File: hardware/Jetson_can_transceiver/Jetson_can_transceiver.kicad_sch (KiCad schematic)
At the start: 5 parts, among them U1 MCP2551-I-P, U2 MCP2551-I-P

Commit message: Added realistic footprints to electronic components
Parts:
- C2: footprint (none) -> Capacitor_SMD:C_0805_2012Metric
- R1, R2: footprint (none) -> Resistor_SMD:R_0805_2012Metric
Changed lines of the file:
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@@
 			)
 		)
-		(property "Footprint" ""
+		(property "Footprint" "Capacitor_SMD:C_0805_2012Metric"
 			(at 83.5152 29.21 0)
 			(effects
@@
 			)
 		)
-		(property "Footprint" ""
+		(property "Footprint" "Resistor_SMD:R_0805_2012Metric"
 			(at 107.188 64.77 90)
 			(effects
@@
 			)
 		)
-		(property "Footprint" ""
+		(property "Footprint" "Resistor_SMD:R_0805_2012Metric"
 			(at 60.198 63.5 90)
 			(effects

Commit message: Completed blueprint for 2 transceivers
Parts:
- added J1: Conn_02x20_Odd_Even, symbol Connector_Generic:Conn_02x20_Odd_Even
- added R3, R4: 120R, Resistor_SMD:R_0805_2012Metric, symbol Device:R
- C2: value 100pF -> 100nF
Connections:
- net GND: now also J1.6 (Pin_6)
- net CANL1: now reaches U2.6 (CANL)
- net CANL1: now also R4.2
- net CANH1: now reaches U2.7 (CANH)
- net CANH1: now also R4.1
- net CANL0: now reaches U1.6 (CANL)
- net CANL0: now also R3.2
- net CANH0: now reaches U1.7 (CANH)
- net CANH0: now also R3.1
- net +5V renamed 5V
- net 5V: now also J1.2 (Pin_2)
- net RXD_1 renamed RX0
- net RX0: now also J1.29 (Pin_29)
- net RXD_2 renamed RX1
- net RX1: now also J1.37 (Pin_37)
- net TXD_1 renamed TX0
- net TX0: now also J1.31 (Pin_31)
- net TXD_2 renamed TX1
- net TX1: now also J1.33 (Pin_33)
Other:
- moved on the sheet: R1, R2, U1, U2

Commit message: added footprints
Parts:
- J1: footprint (none) -> Connector_Harwin:Harwin_M20-7812045_2x20_P2.54mm_Vertical
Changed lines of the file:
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@@
 			)
 		)
-		(property "Footprint" ""
+		(property "Footprint" "Connector_Harwin:Harwin_M20-7812045_2x20_P2.54mm_Vertical"
 			(at 83.82 99.06 0)
 			(effects

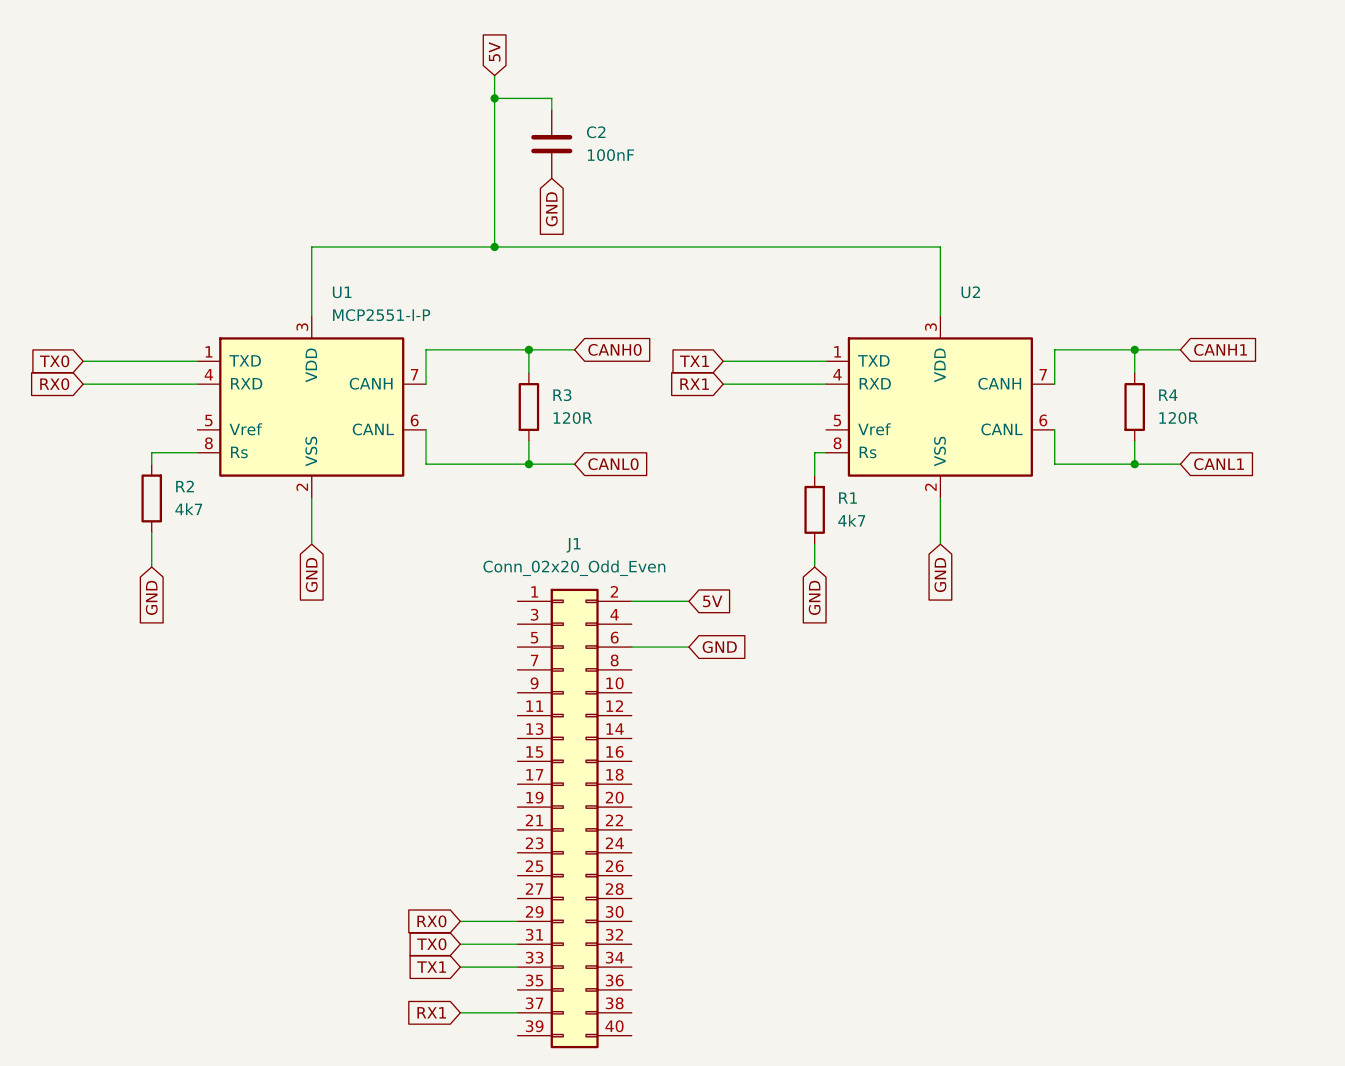
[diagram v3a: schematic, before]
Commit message: Changed from mcp2551 to mcp2542fd, added test points, changed footprint to 0603
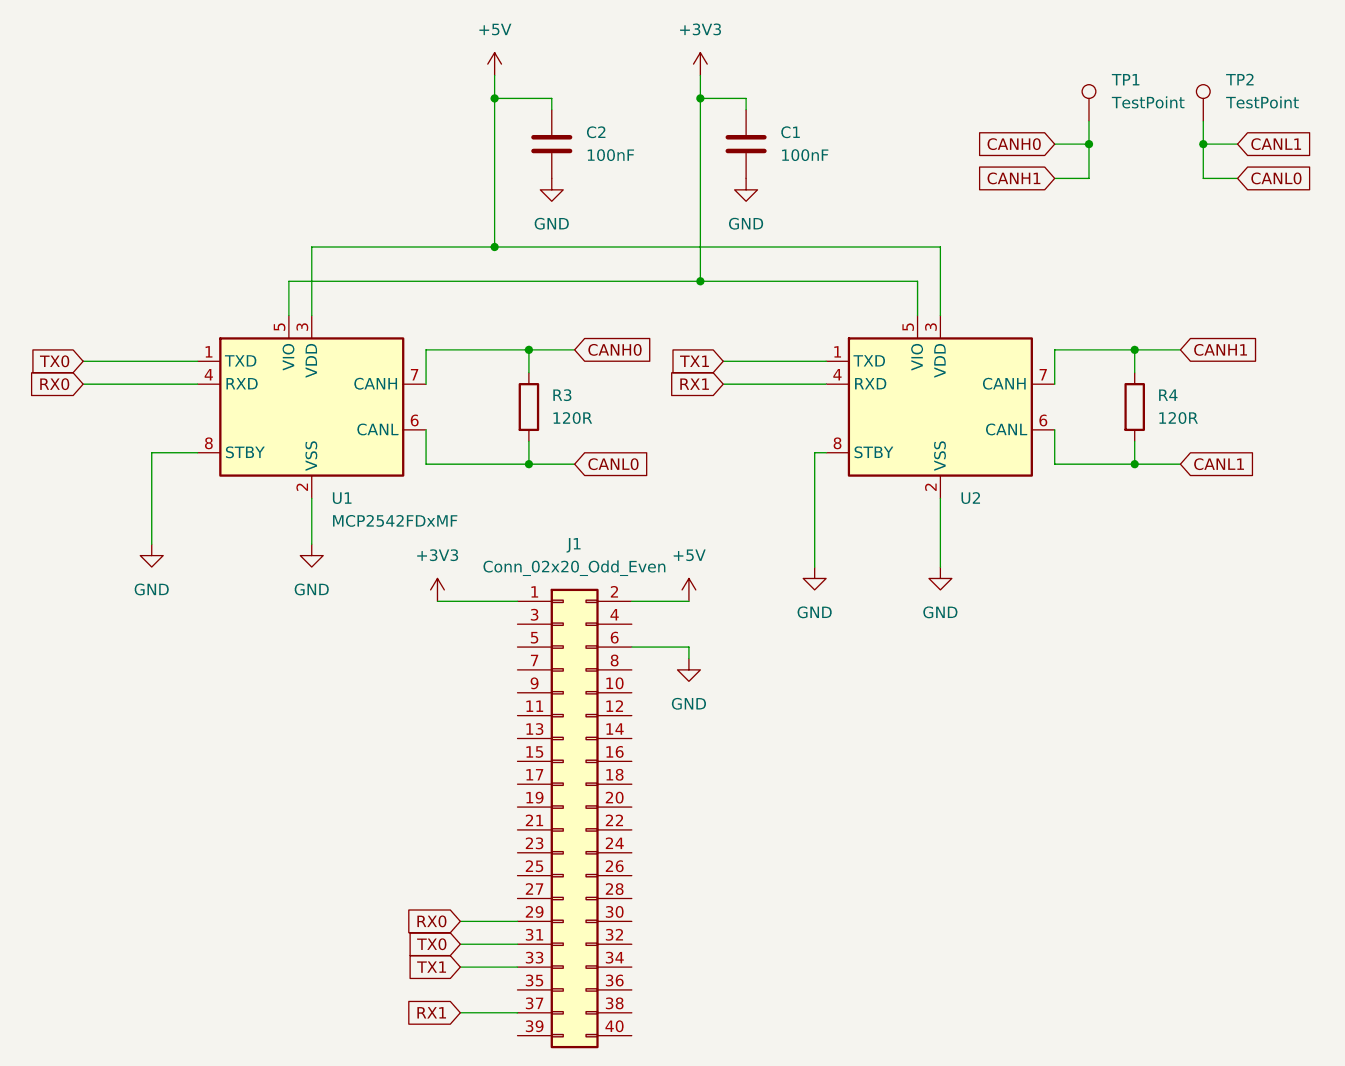
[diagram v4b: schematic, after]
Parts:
- removed R1, R2: 4k7, Resistor_SMD:R_0805_2012Metric, symbol Device:R
- removed U1, U2: MCP2551-I-P, Package_DIP:DIP-8_W7.62mm, symbol Interface_CAN_LIN:MCP2551-I-P
- added C1: 100nF, Capacitor_SMD:C_0603_1608Metric, symbol Device:C
- added TP1, TP2: TestPoint, S1751-46R:HARWIN_S1751-46R, symbol Connector:TestPoint
- added U1, U2: MCP2542FDxMF, Package_DFN_QFN:DFN-8-1EP_3x3mm_P0.65mm_EP1.55x2.4mm, symbol Interface_CAN_LIN:MCP2542FDxMF
- C2: footprint Capacitor_SMD:C_0805_2012Metric -> Capacitor_SMD:C_0603_1608Metric
- R3, R4: footprint Resistor_SMD:R_0805_2012Metric -> Resistor_SMD:R_0603_1608Metric
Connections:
- net CANH1 is gone; now on net CANH0: R4.1
- net CANL1 is gone; now on net CANL0: R4.2
- net CANH0: now also TP1.1, U1.7 (CANH), U2.7 (CANH)
- net CANL0: now also TP2.1, U1.6 (CANL), U2.6 (CANL)
- net GND: now also C1.2, U1.2 (VSS), U1.8 (STBY), U1.9 (VSS), U2.2 (VSS), U2.8 (STBY), U2.9 (VSS)
- net RX0: now also U1.4 (RXD)
- net RX1: now also U2.4 (RXD)
- net TX0: now also U1.1 (TXD)
- net TX1: now also U2.1 (TXD)
- net +3V3: now reaches J1.1 (Pin_1)
- net +3V3: now also C1.1, U1.5 (VIO), U2.5 (VIO)
- net 5V renamed +5V
- net +5V: now also U1.3 (VDD), U2.3 (VDD)
